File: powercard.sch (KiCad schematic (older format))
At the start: 6 parts, among them J1 EDGE, J3 DBG

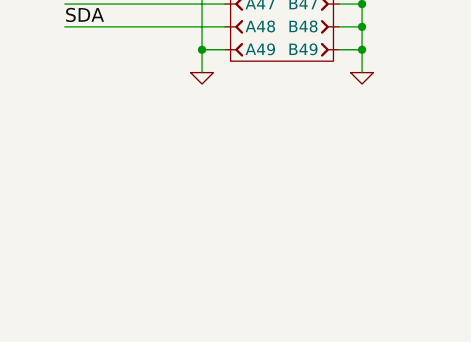
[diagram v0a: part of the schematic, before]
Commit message: Layout tweaks
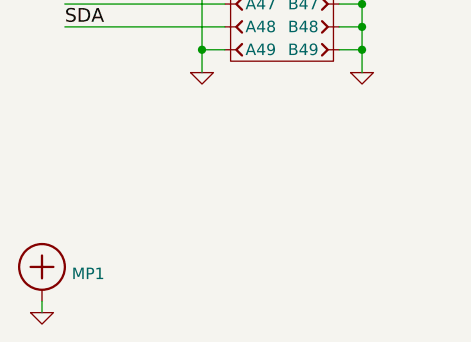
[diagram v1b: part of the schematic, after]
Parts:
- added MP1: SCREW, mech:SCREW-3-SUPPORTED, symbol SCREW
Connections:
- net GND: now also MP1.1
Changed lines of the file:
@@
 SDA
 $Comp
-L GND #PWR1
+L GND #PWR2
 U 1 1 57746E13
 P 1600 6500
-F 0 "#PWR1" H 1600 6500 30  0001 C CNN
+F 0 "#PWR2" H 1600 6500 30  0001 C CNN
 F 1 "GND" H 1600 6430 30  0001 C CNN
 F 2 "" H 1600 6500 60  0000 C CNN
@@
 $EndComp
 $Comp
-L GND #PWR3
+L GND #PWR4
 U 1 1 5776D741
 P 10200 3000
-F 0 "#PWR3" H 10200 3000 30  0001 C CNN
+F 0 "#PWR4" H 10200 3000 30  0001 C CNN
 F 1 "GND" H 10200 2930 30  0001 C CNN
 F 2 "" H 10200 3000 60  0000 C CNN
@@
 $EndComp
 $Comp
-L GND #PWR2
+L GND #PWR3
 U 1 1 5776E55B
 P 2300 6500
-F 0 "#PWR2" H 2300 6500 30  0001 C CNN
+F 0 "#PWR3" H 2300 6500 30  0001 C CNN
 F 1 "GND" H 2300 6430 30  0001 C CNN
 F 2 "" H 2300 6500 60  0000 C CNN
@@
 	10800 2000 10800 1900
 $Comp
-L GND #PWR4
+L GND #PWR5
 U 1 1 577561CC
 P 10400 2250
-F 0 "#PWR4" H 10400 2250 30  0001 C CNN
+F 0 "#PWR5" H 10400 2250 30  0001 C CNN
 F 1 "GND" H 10400 2180 30  0001 C CNN
 F 2 "" H 10400 2250 60  0000 C CNN
@@
 	10400 2250 10400 2200
 $Comp
-L GND #PWR5
+L GND #PWR6
 U 1 1 5775647A
 P 10800 2250
-F 0 "#PWR5" H 10800 2250 30  0001 C CNN
+F 0 "#PWR6" H 10800 2250 30  0001 C CNN
 F 1 "GND" H 10800 2180 30  0001 C CNN
 F 2 "" H 10800 2250 60  0000 C CNN
@@
 Wire Wire Line
 	10800 2250 10800 2200
+$Comp
+L SCREW MP1
+U 1 1 5775DDCC
+P 900 7350
+F 0 "MP1" H 1030 7320 50  0000 L CNN
+F 1 "SCREW" H 1030 7275 50  0001 L CNN
+F 2 "mech:SCREW-3-SUPPORTED" H 900 7350 50  0001 C CNN
+F 3 "" H 900 7350 60  0000 C CNN
+	1    900  7350
+	1    0    0    -1
+$EndComp
+$Comp
+L GND #PWR1
+U 1 1 5775E26A
+P 900 7550
+F 0 "#PWR1" H 900 7550 30  0001 C CNN
+F 1 "GND" H 900 7480 30  0001 C CNN
+F 2 "" H 900 7550 60  0000 C CNN
+F 3 "" H 900 7550 60  0000 C CNN
+	1    900  7550
+	1    0    0    -1
+$EndComp
+Wire Wire Line
+	900  7550 900  7500
 $EndSCHEMATC

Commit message: More PCB tweaks
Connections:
- net GND: now also J1.A45, J1.A46; no longer J1.A49
- net INT#: now also J1.A47; no longer J1.A46
- net SCL: now also J1.A48; no longer J1.A47
- net SDA: now also J1.A49; no longer J1.A48
- net Controller/DBGRX renamed Supervisor/DBGRX
- net Controller/DBGTX renamed Supervisor/DBGTX
- net Controller/LED_G renamed Supervisor/LED_G
- net Controller/LED_R renamed Supervisor/LED_R
- no-connect marks 1 -> 0

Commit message: Commit R1.0 sent to fab
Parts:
- removed DS1: R, smd-semi:LED-0603, symbol LED-0603
- removed DS2: G, smd-semi:LED-0603, symbol LED-0603
- removed R33, R34: 2k2, IPC7351-Nominal:RESC1608X50, symbol R-0603
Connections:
- net 3V3SENSE_1: now also J1.A36; no longer J1.A34
- net 3V3SENSE_2: now also J1.A37; no longer J1.A24
- net 5VSENSE_2: now also J1.A14; no longer J1.A2
- net GND: now also J1.A2, J1.A24, J1.A34; no longer J1.A14, J1.A36, J1.A37
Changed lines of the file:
@@
 Text Label 1000 2600 0    60   ~ 0
 5VSENSE_1
-Text Label 1000 1400 0    60   ~ 0
+Text Label 1000 2700 0    60   ~ 0
 5VSENSE_2
-Text Label 1000 4900 0    60   ~ 0
+Text Label 1000 5100 0    60   ~ 0
 3V3SENSE_1
-Text Label 1000 3800 0    60   ~ 0
+Text Label 1000 5200 0    60   ~ 0
 3V3SENSE_2
 Text Label 1000 5900 0    60   ~ 0
@@
 F16 "DBGRX" I R 10100 2700 60
 F17 "INT#" O R 10100 1200 60
-F18 "LED_G" O R 10100 1500 60
-F19 "LED_R" O R 10100 1600 60
 $EndSheet
 Text Label 4800 6200 0    60   ~ 0
@@
 INT#
 $Comp
-L LED-0603 DS1
-U 1 1 57754CCF
-P 10400 2100
-F 0 "DS1" H 10550 2146 50  0000 L CNN
-F 1 "R" H 10550 2055 50  0000 L CNN
-F 2 "smd-semi:LED-0603" H 10400 1950 50  0001 C CNN
-F 3 "" H 10400 2100 60  0000 C CNN
-F 4 "LED RED [0603]" H 10400 1850 60  0001 C CNN "BOM"
-	1    10400 2100
-	1    0    0    -1
-$EndComp
-$Comp
-L LED-0603 DS2
-U 1 1 577551CD
-P 10800 2100
-F 0 "DS2" H 10950 2146 50  0000 L CNN
-F 1 "G" H 10950 2055 50  0000 L CNN
-F 2 "smd-semi:LED-0603" H 10800 1950 50  0001 C CNN
-F 3 "" H 10800 2100 60  0000 C CNN
-F 4 "LED GREEN [0603]" H 10800 1850 60  0001 C CNN "BOM"
-	1    10800 2100
-	1    0    0    -1
-$EndComp
-$Comp
-L R-0603 R33
-U 1 1 577559F9
-P 10400 1800
-F 0 "R33" H 10463 1846 50  0000 L CNN
-F 1 "2k2" H 10463 1755 50  0000 L CNN
-F 2 "IPC7351-Nominal:RESC1608X50" H 10400 1800 50  0001 C CNN
-F 3 "" H 10400 1850 60  0000 C CNN
-F 4 "RES SMD 2k2 1% [0603]" H 11150 2350 60  0001 C CNN "BOM"
-	1    10400 1800
-	1    0    0    -1
-$EndComp
-$Comp
-L R-0603 R34
-U 1 1 57755F10
-P 10800 1800
-F 0 "R34" H 10863 1846 50  0000 L CNN
-F 1 "2k2" H 10863 1755 50  0000 L CNN
-F 2 "IPC7351-Nominal:RESC1608X50" H 10800 1800 50  0001 C CNN
-F 3 "" H 10800 1850 60  0000 C CNN
-F 4 "RES SMD 2k2 1% [0603]" H 11550 2350 60  0001 C CNN "BOM"
-	1    10800 1800
-	1    0    0    -1
-$EndComp
-$Comp
-L GND #PWR5
-U 1 1 577561CC
-P 10400 2250
-F 0 "#PWR5" H 10400 2250 30  0001 C CNN
-F 1 "GND" H 10400 2180 30  0001 C CNN
-F 2 "" H 10400 2250 60  0000 C CNN
-F 3 "" H 10400 2250 60  0000 C CNN
-	1    10400 2250
-	1    0    0    -1
-$EndComp
-$Comp
-L GND #PWR6
-U 1 1 5775647A
-P 10800 2250
-F 0 "#PWR6" H 10800 2250 30  0001 C CNN
-F 1 "GND" H 10800 2180 30  0001 C CNN
-F 2 "" H 10800 2250 60  0000 C CNN
-F 3 "" H 10800 2250 60  0000 C CNN
-	1    10800 2250
-	1    0    0    -1
-$EndComp
-$Comp
 L SCREW MP1
 U 1 1 5775DDCC
@@
 	1    0    0    -1
 $EndComp
+Text Label 4800 2400 0    60   ~ 0
+5VSENSE_1
+Text Label 4800 1100 0    60   ~ 0
+5VSENSE_2
 Wire Wire Line
 	2200 1300 5400 1300
@@
 Connection ~ 2300 5900
 Wire Wire Line
-	900  1400 1700 1400
-Wire Wire Line
-	900  2600 1700 2600
-Wire Wire Line
-	1000 3800 1700 3800
-Wire Wire Line
-	1000 4900 1700 4900
+	1000 2700 1700 2700
+Wire Wire Line
+	1000 5200 1700 5200
+Wire Wire Line
+	1000 5100 1700 5100
 Wire Wire Line
 	1000 5900 1700 5900
@@
 Connection ~ 1600 2500
 Wire Wire Line
-	1600 2700 1700 2700
-Connection ~ 1600 2700
-Wire Wire Line
 	1700 2900 1600 2900
 Connection ~ 1600 2900
@@
 Connection ~ 1600 5000
 Wire Wire Line
-	1600 5200 1700 5200
-Connection ~ 1600 5200
-Wire Wire Line
 	1700 5300 1600 5300
 Connection ~ 1600 5300
@@
 Connection ~ 1600 5800
 Wire Wire Line
-	5400 1100 900  1100
-Wire Wire Line
-	900  1100 900  1400
-Wire Wire Line
-	5400 2400 900  2400
-Wire Wire Line
-	900  2400 900  2600
-Wire Wire Line
 	7600 3700 6800 3700
 Wire Wire Line
@@
 	6800 3900 7900 3900
 Wire Wire Line
-	7900 3900 7900 1700
+	7900 1700 7900 6100
 Wire Wire Line
 	7900 1700 8700 1700
@@
 	8700 1900 8100 1900
 Wire Wire Line
-	8100 1900 8100 6100
-Wire Wire Line
 	8100 5000 6800 5000
-Connection ~ 8100 5000
 Wire Wire Line
 	8700 1000 8200 1000
 Wire Wire Line
-	8100 6100 6800 6100
+	7900 6100 6800 6100
 Wire Wire Line
 	6800 6200 8200 6200
@@
 	10200 2900 10300 2900
 Wire Wire Line
-	2300 6500 2300 6100
+	2300 6100 2300 6500
 Wire Wire Line
 	2300 6100 2200 6100
@@
 Connection ~ 1600 4000
 Wire Wire Line
-	1700 5100 1600 5100
-Connection ~ 1600 5100
-Wire Wire Line
 	1000 6200 1700 6200
 Wire Wire Line
 	10500 1200 10100 1200
-Wire Wire Line
-	10100 1600 10400 1600
-Wire Wire Line
-	10400 1600 10400 1700
-Wire Wire Line
-	10100 1500 10800 1500
-Wire Wire Line
-	10800 1500 10800 1700
-Wire Wire Line
-	10400 2000 10400 1900
-Wire Wire Line
-	10800 2000 10800 1900
-Wire Wire Line
-	10400 2250 10400 2200
-Wire Wire Line
-	10800 2250 10800 2200
 Wire Wire Line
 	900  7550 900  7500
@@
 	1700 6100 1600 6100
 Connection ~ 1600 6100
+Wire Wire Line
+	4800 1100 5400 1100
+Wire Wire Line
+	4800 2400 5400 2400
+Wire Wire Line
+	1000 2600 1700 2600
+Wire Wire Line
+	1700 1400 1600 1400
+Connection ~ 1600 1400
+Wire Wire Line
+	1700 4900 1600 4900
+Connection ~ 1600 4900
+Wire Wire Line
+	1700 3800 1600 3800
+Connection ~ 1600 3800
+Wire Wire Line
+	8100 1900 8100 5000
+Connection ~ 7900 3900
 $EndSCHEMATC
